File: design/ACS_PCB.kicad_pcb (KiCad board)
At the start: 6 copper layers, 60 x 60 mm, 98 parts, among them CN2 jst sh 6 pin, J2 GT-USB-7010ASV, J4 ARM standard debug, Q1 NPN, Q2 NPN, Q3 NPN, Q4 NPN, U1 USBLC6-2SC6, U10 ME6206B18XG, U2 STM32F405RGTx, U3 SN65HVD232DR, U4 2.54_conn 12 pin, U5 ICM-20948, U6 TPS56A37RPAR, U7 MS5611-01BA, U8 LM2596S-3.3_C19631822, Y1 16MHz

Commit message: finished layout
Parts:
- removed CN2: jst sh 6 pin, EasyEDA:CONN-SMD_6P-P1.00_C9900032244
- removed CN_I2C_1, CN_I2C_2, CN_UART1: JST_GH 4, EasyEDA:CONN-SMD_4P-P1.25_JXTCONN_DMX-4PWB-43
- removed D5, D6, D7: SS34, EasyEDA:SMC_L6.9-W5.9-LS7.9-RD
- removed R17, R20: 5k1, Resistor_SMD:R_0603_1608Metric
- removed R23: 10k, Resistor_SMD:R_0603_1608Metric
- removed SW_BUTTON1: Button, EasyEDA:SW-SMD_4P-L5.2-W5.2-P3.70-LS6.4
- added H5: MountingHole_Pad, MountingHole:MountingHole_2.2mm_M2_DIN965_Pad, F.Cu at (128.0, 72.0)
- BUZZER1, C1, C11, C12, C16, C17, C18, C20, C21, C22, C23, C24, C5, C7, C8, D3, D4, D8, F1, F2, F3, J2, L2, L3, Q4, R1, R12, R15, R16, R18, R19, R22, R24, R26, R27, R28, R5, R6, R7, U1, U6, U8: moved to B.Cu
- moved Q1 152.0 mm to (115.0, 116.5), turned to -90 degrees
- moved Q3 142.5 mm to (121.5, 116.5), turned to -90 degrees
- moved Q2 138.5 mm to (128.0, 116.5), turned to -90 degrees
- moved U1 138.5 mm to (169.9, 95.5), turned to 90 degrees
- moved U3 135.0 mm to (161.6, 101.5)
- moved D4 131.0 mm to (158.0, 71.5), turned to -90 degrees
- moved Q4 130.1 mm to (123.5, 87.0)
- moved F3 127.3 mm to (164.0, 72.5), turned to -90 degrees
- moved F2 119.5 mm to (154.0, 87.7), turned to 90 degrees
- moved R8 117.9 mm to (116.5, 120.5), turned to 90 degrees
- moved R9 117.1 mm to (114.0, 120.5), turned to 90 degrees
- moved C16 117.0 mm to (179.0, 120.0), turned to 0 degrees
- moved R12 116.0 mm to (175.5, 126.5), turned to -90 degrees
- moved C12 115.2 mm to (154.5, 83.0), turned to 0 degrees
- moved C11 114.8 mm to (154.5, 81.0), turned to 0 degrees
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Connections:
- R13 pad 1: +3V3 -> +3.3V
- U2 pad 29: /EXT_SCL -> unconnected-(U2-PB10-Pad29)
- U2 pad 30: /EXT_SDA -> unconnected-(U2-PB11-Pad30)
- U2 pad 42: /UART_TX -> unconnected-(U2-PA9-Pad42)
- U2 pad 43: /UART_RX -> unconnected-(U2-PA10-Pad43)
- U2 pad 9: /BUTTON_SENSE -> unconnected-(U2-PC1-Pad9)
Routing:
- net GND: track 62.1 -> 185.2 mm, vias 33 -> 79
- net VCC: track 0.00 -> 90.7 mm, vias 0 -> 1
- net /BOOT0: track 0.00 -> 49.1 mm, vias 0 -> 2
- net /SWCLK: track 0.00 -> 48.4 mm, vias 0 -> 2
- net /PWM_SERVO_4: track 0.00 -> 46.8 mm
- net /SWDIO: track 0.00 -> 45.2 mm, vias 0 -> 2
- net /NRST: track 0.00 -> 44.7 mm, vias 0 -> 2
- net /PWM_SERVO_3: track 0.00 -> 43.2 mm
- net /LEDG_CTRL: track 0.00 -> 41.1 mm, vias 0 -> 2
- net /LEDB_CTRL: track 0.00 -> 36.6 mm, vias 0 -> 2
- net /MISO: track 0.00 -> 34.7 mm, vias 0 -> 3
- net /CAN_L: track 0.00 -> 33.1 mm, vias 0 -> 1
- net /CAN_H: track 0.00 -> 32.1 mm, vias 0 -> 1
- net /CAN_RX: track 0.00 -> 31.8 mm, vias 0 -> 2
- net /PWM_SERVO_2: track 0.00 -> 31.2 mm
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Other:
- board size 60 x 60 mm -> 80 x 80 mm

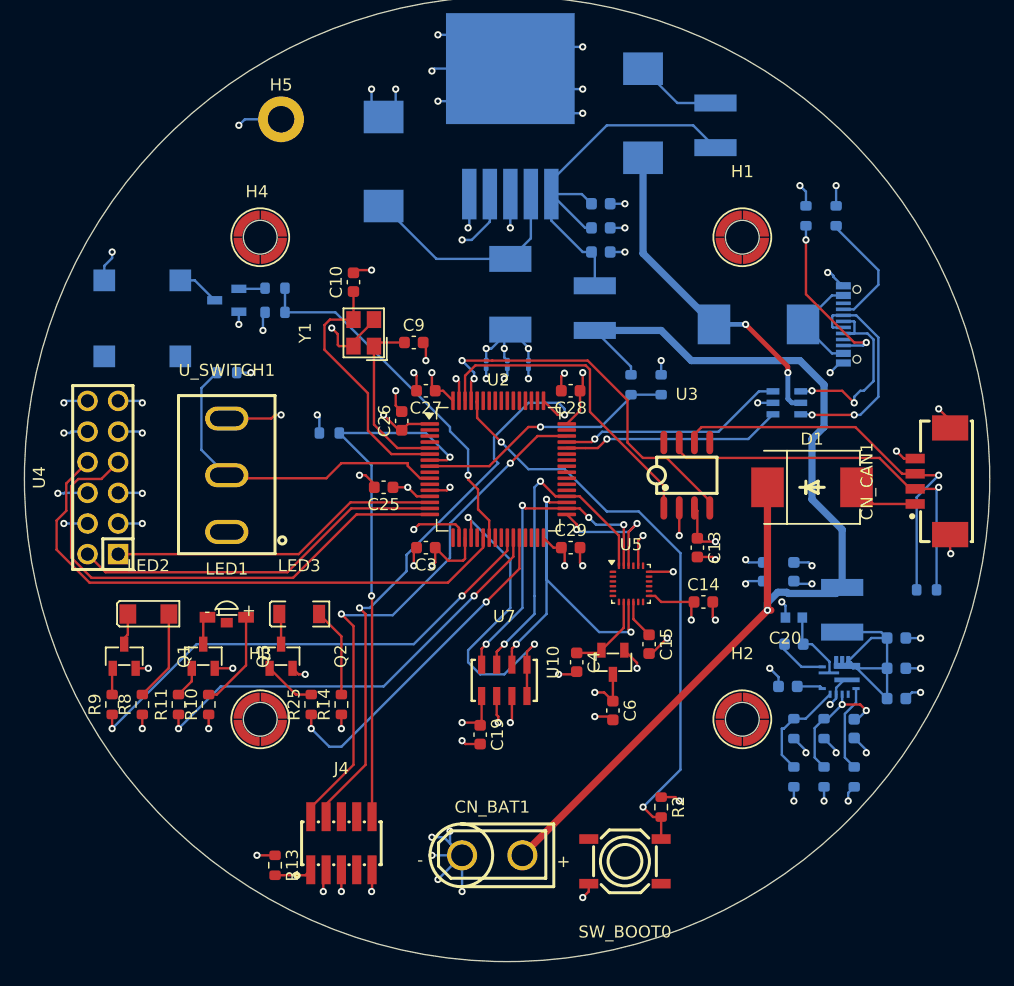
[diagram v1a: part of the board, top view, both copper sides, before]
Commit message: fixed silkscreen texts
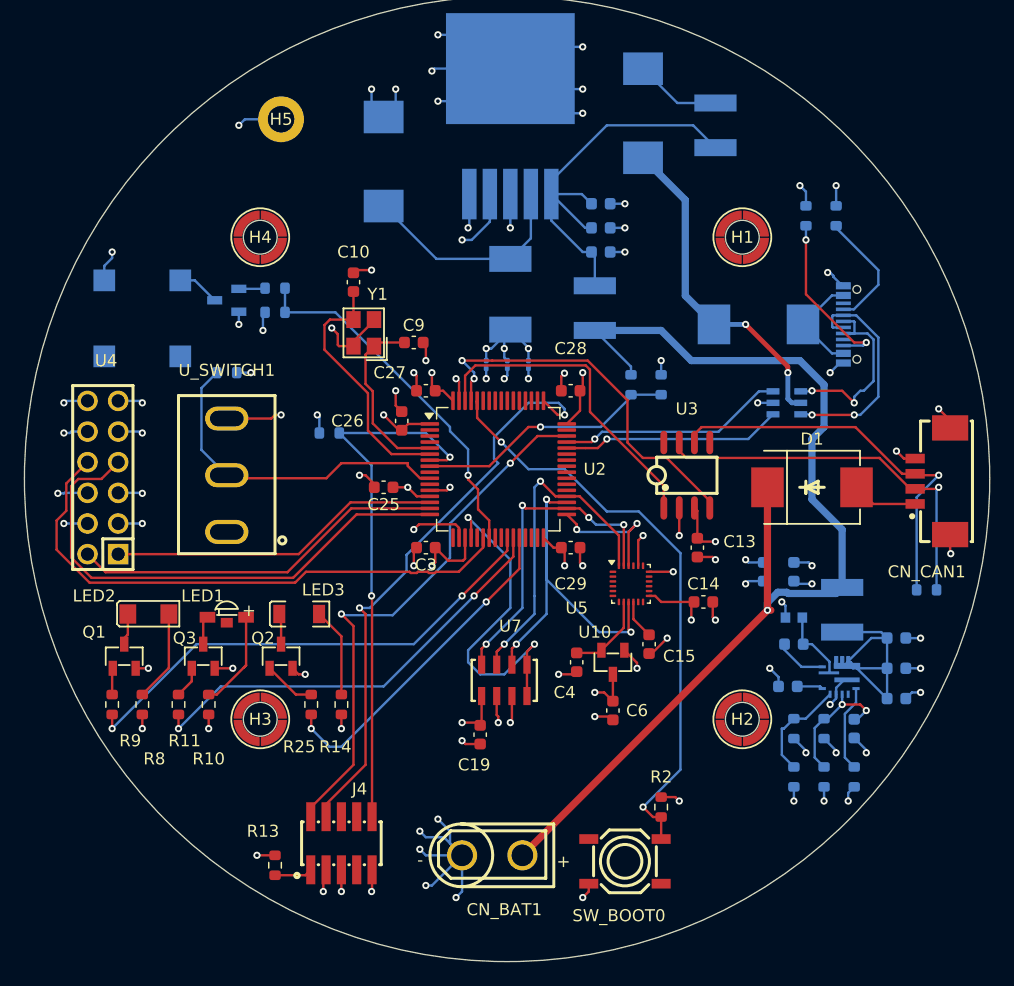
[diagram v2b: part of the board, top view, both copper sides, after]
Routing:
- net GND: track 185.2 -> 190.9 mm
- net /OSC_IN: track 14.6 -> 15.2 mm

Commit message: added graphics
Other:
- board text added: "Sköll v1.0 Fabian Andersson 2025-10-14"

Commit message: changed to 4 layers
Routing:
- net +6V: track 20.5 -> 190.5 mm, vias 13 -> 7
- net VCC: track 90.7 -> 91.3 mm
- removed copper zone on In3.Cu, net +6V
- removed copper zone on In4.Cu, net GND
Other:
- copper layers 6 -> 4

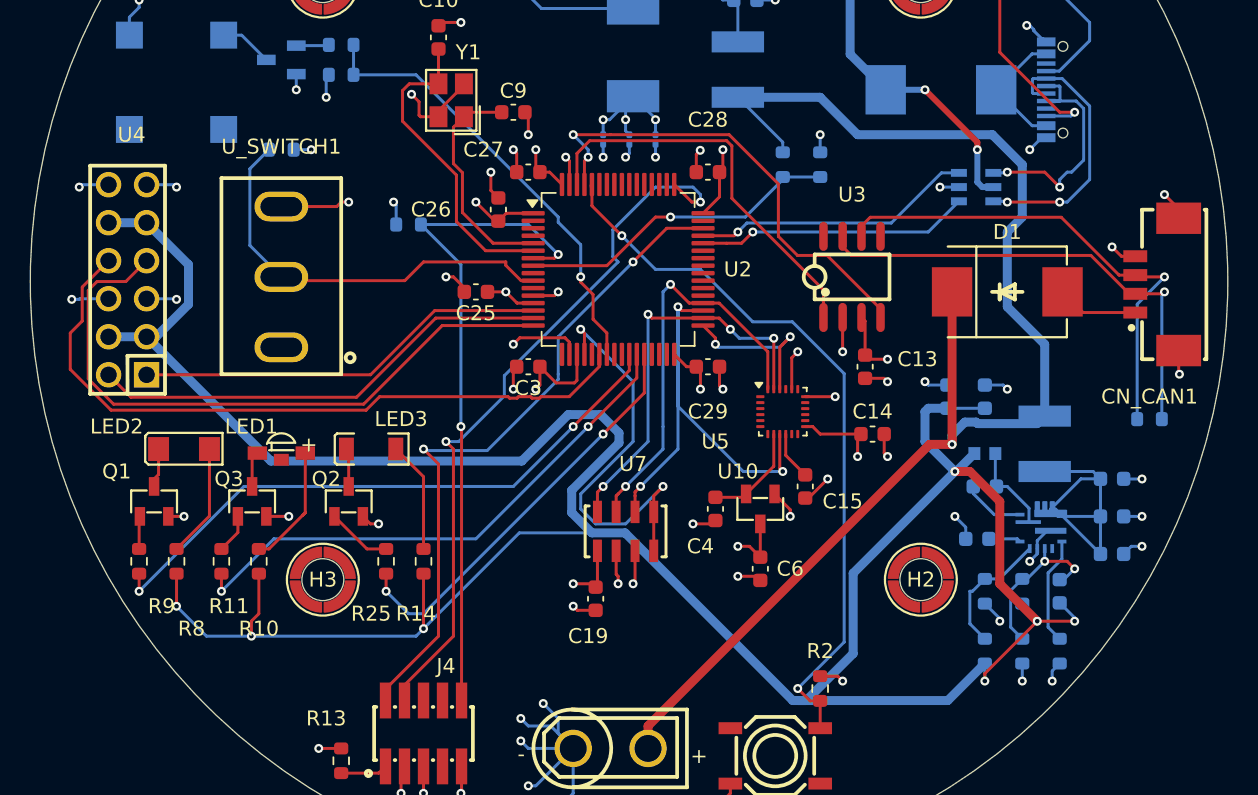
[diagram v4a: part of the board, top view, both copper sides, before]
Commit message: fixed layout review things (ish)
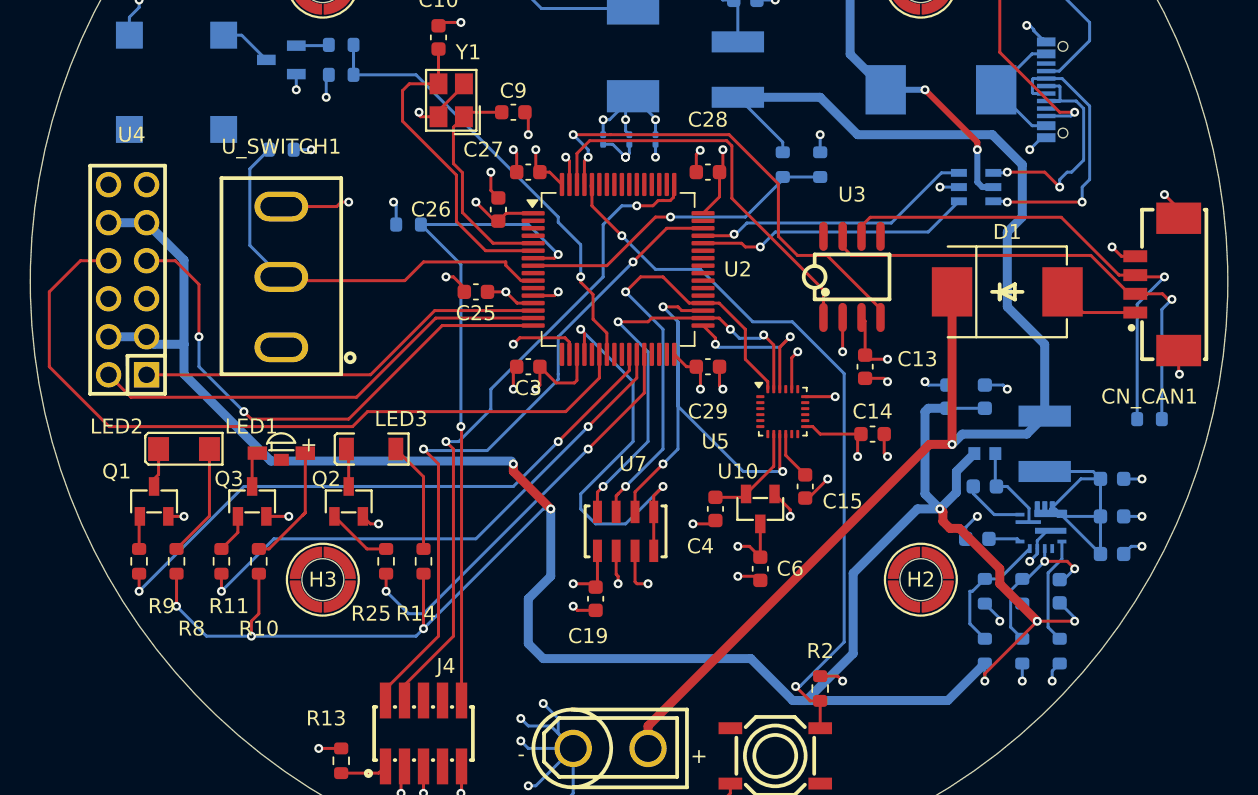
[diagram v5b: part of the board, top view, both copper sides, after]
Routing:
- net GND: track 190.9 -> 182.7 mm, vias 79 -> 75
- net /PWM_SERVO_3: track 43.2 -> 36.0 mm, vias 0 -> 2
- net /PWM_SERVO_4: track 47.0 -> 51.1 mm
- net +6V: track 190.5 -> 186.4 mm, vias 7 -> 9
- net /MOSI: track 27.6 -> 31.5 mm
- net /SWCLK: track 48.4 -> 44.6 mm
- net /SCK: track 27.1 -> 29.3 mm
- net /USB_ESD-: track 18.4 -> 19.0 mm

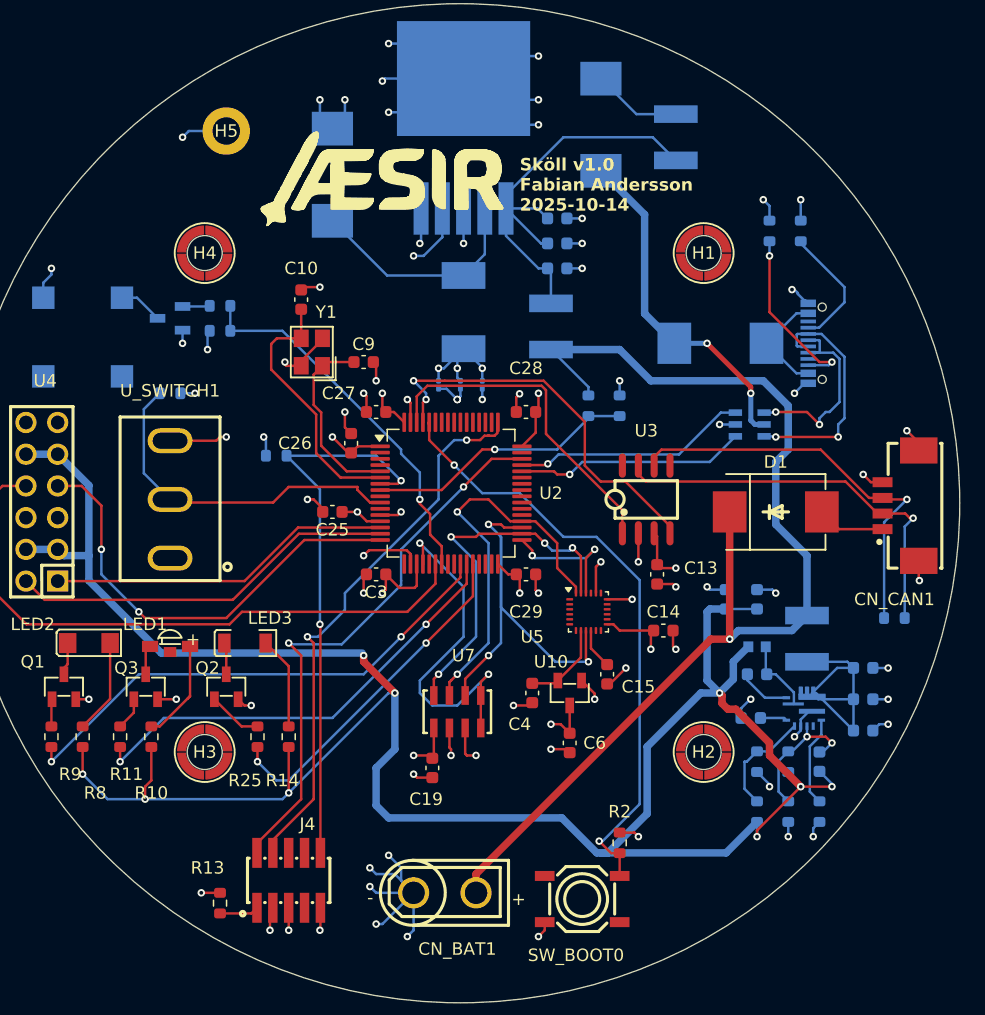
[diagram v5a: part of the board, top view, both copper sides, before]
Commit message: fixed some of the suggestions by reviewers
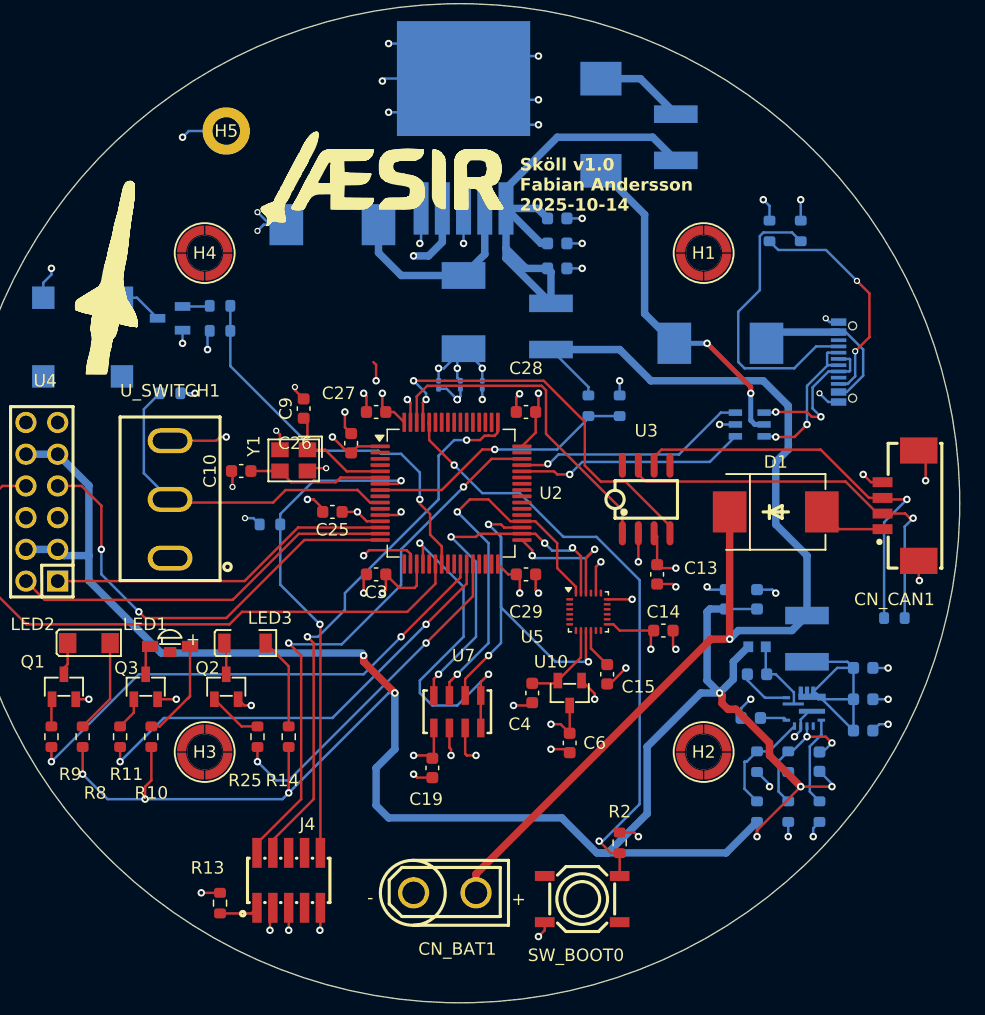
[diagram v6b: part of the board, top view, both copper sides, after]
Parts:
- moved C10 14.5 mm to (129.2, 99.2), turned to 180 degrees
- moved Y1 8.79 mm to (133.4, 98.4), turned to 180 degrees
- moved C9 6.08 mm to (134.2, 94.2), turned to 90 degrees
- moved R1 5.52 mm to (131.5, 103.5)
- moved D3 4.00 mm to (136.5, 79.5), turned to 180 degrees
- moved J2 2.86 mm to (179.4, 90.5)
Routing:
- net GND: track 182.7 -> 163.1 mm, vias 75 -> 72
- net Net-(J2-CC1): track 10.1 -> 23.6 mm
- net /OSC_OUT: track 21.1 -> 10.9 mm
- net Net-(U8-Vin): track 35.0 -> 42.9 mm
- net /USB_ESD-: track 19.0 -> 12.1 mm
- net /OSC_IN: track 15.2 -> 9.19 mm
- net Net-(D8-A): track 8.67 -> 13.3 mm
- net Net-(J2-CC2): track 14.3 -> 18.4 mm
- net /USB_ESD+: track 16.5 -> 12.8 mm
- net /NRST: track 44.7 -> 41.0 mm
- net /OUTPUT: track 18.4 -> 15.9 mm
- net /PWM_BUZZER: track 30.1 -> 31.6 mm
